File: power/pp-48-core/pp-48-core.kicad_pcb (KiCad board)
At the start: 4 copper layers, 56 x 72 mm, 74 parts, among them J1 XT30PW-M, J2 CTRL IN, J3 CTRL OUT, J301 CHAIN OUT, J4 12V AUX OUT, J5 SWD, Q1 2N7002, Q6 2N7002, U1 LM5164DDA, U2 URB4812YMD-6WR3, U3 STM32G070CBT6, U4 ISO1640BD, U5 ISO7721D, U6 TCA9548APWR, Y1 8MHz

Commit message: pp-48 plane boards: press deadline line (docs/press-deadline-line.md decided: option B + A) on a 14-pin chain (S14B-PH-K-S C157938; 13 PRESS_EN, 14 EXP_RSTN, cable n -> 15 - n, pins v 35..61); unit Q10 / R31 switch the photoMOS LED returns (PRESS_RTN), core U301 74LVC1G123 deadline (pp:74LVC1G123 single-unit copy) on PC6 PRESS_TRIG, PC7 EXP_RSTN to the units' /RESET; ERC 0 both; boards rebuilt and placed, unit 78.5 x 72 with the strip power path re-placed top-down; unit routing tools (route_unit.py hand copper + In2 band / +3V3 trunk, unitsplit.py, route_unit.sh flow): DRC 0 errors, ~10 unconnected at expander U5; core placed, not routed; pmmount.py restored from granite_controller; ADR 0005 decision 4; handoff
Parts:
- added C301: 10u, Capacitor_SMD:C_0805_2012Metric, F.Cu at (95.0, 163.6)
- added C302: 100n, Capacitor_SMD:C_0402_1005Metric, F.Cu at (95.0, 157.2)
- added R301: 100k, Resistor_SMD:R_0402_1005Metric, F.Cu at (98.6, 160.0)
- added R302: 100k, Resistor_SMD:R_0402_1005Metric, F.Cu at (91.6, 159.4)
- added R303: 10k, Resistor_SMD:R_0402_1005Metric, F.Cu at (91.6, 162.6)
- added U301: 74LVC1G123, Package_SO:SSOP-8_2.95x2.8mm_P0.65mm, F.Cu at (95.0, 160.0)
- J301: footprint Connector_JST:JST_PH_S12B-PH-K_1x12_P2.00mm_Horizontal -> Connector_JST:JST_PH_S14B-PH-K_1x14_P2.00mm_Horizontal
- moved J301 4.00 mm to (101.4, 135.0)
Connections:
- J301 pad 1: /UNIT4_SCL -> /EXP_RSTN
- J301 pad 10: /UNIT1_SCL -> /UNIT2_SDA
- J301 pad 11: /UNIT1_SDA -> GND
- J301 pad 12: +3V3 -> /UNIT1_SCL
- J301 pad 2: /UNIT4_SDA -> /Chain/PRESS_EN
- J301 pad 3: GND -> /UNIT4_SCL
- J301 pad 4: /UNIT3_SCL -> /UNIT4_SDA
- J301 pad 5: /UNIT3_SDA -> GND
- J301 pad 6: GND -> /UNIT3_SCL
- J301 pad 7: /UNIT2_SCL -> /UNIT3_SDA
- J301 pad 8: /UNIT2_SDA -> GND
- J301 pad 9: GND -> /UNIT2_SCL
- U3 pad 30: unconnected-(U3-PC6-Pad30) -> /PRESS_TRIG
- U3 pad 31: unconnected-(U3-PC7-Pad31) -> /EXP_RSTN

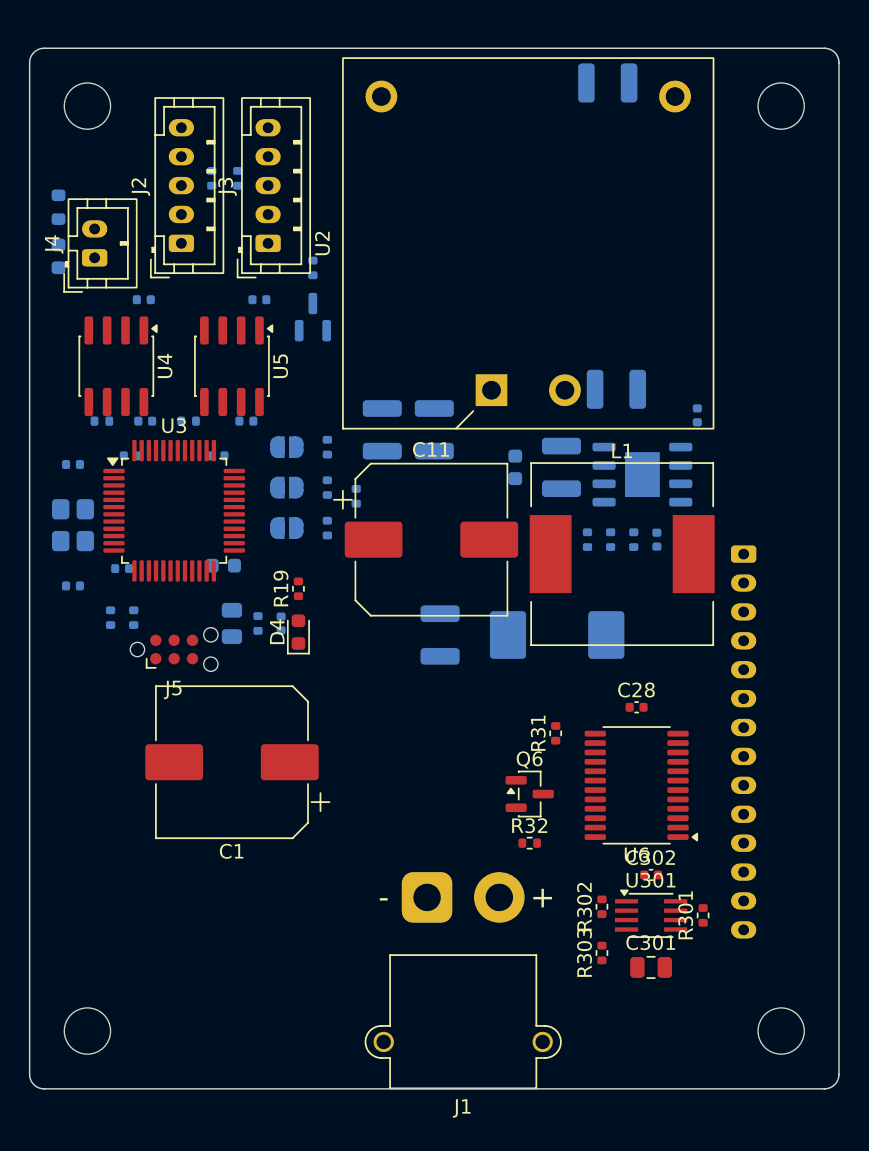
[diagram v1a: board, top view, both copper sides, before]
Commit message: pp-48-core: Fly-Buck placed where the 12 V module was (top right): L2 SRF0703 rot 270 on the corner of a new CTRL_GND island strip along the top edge (diagonal windings: SEC2 in the strip, SW / VOUT1 bus side, CTRL_GND pad an F pocket with vias to In1 / B), secondary D6 / C30 / C31 / D7 in the strip, U2 rot 180 with SW next to L2, its caps and networks on F / B around it; placement DRC 0 errors besides unconnected, parity clean; handoff
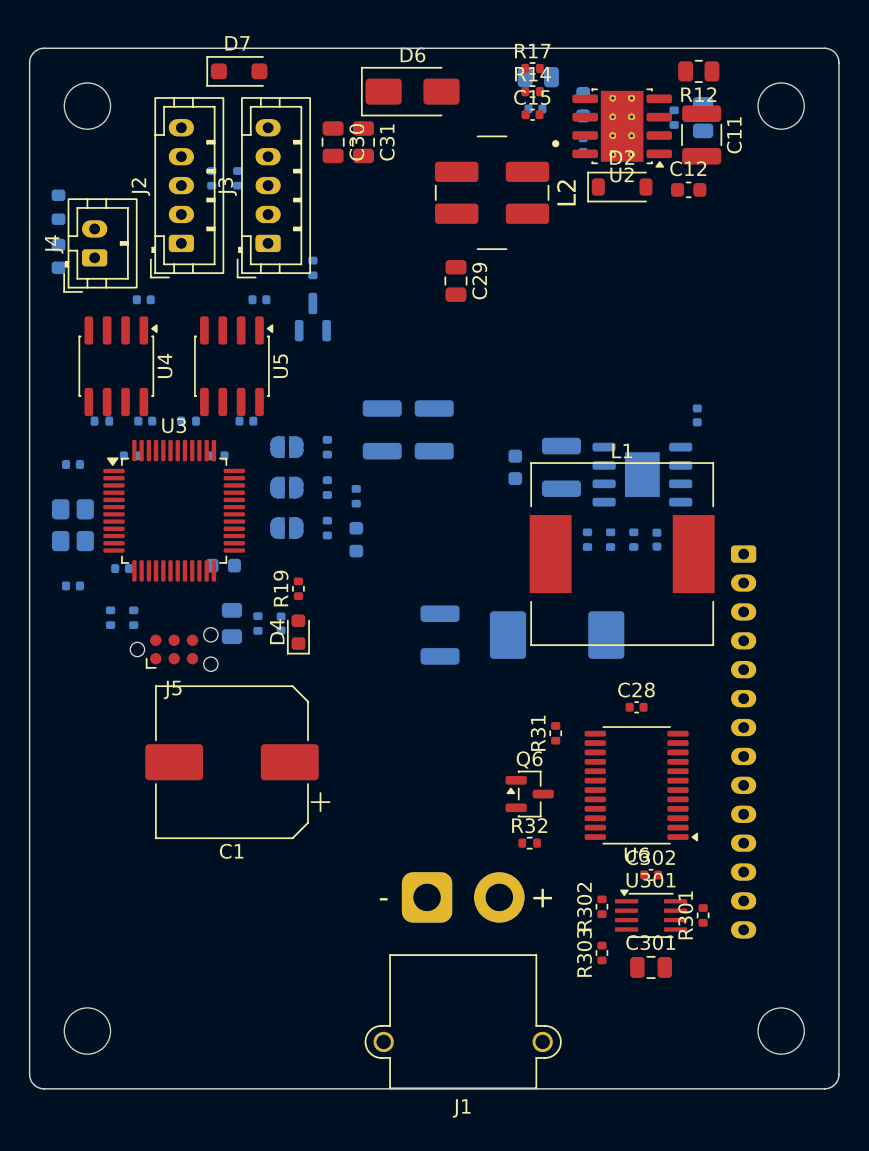
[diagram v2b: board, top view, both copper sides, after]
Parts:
- added C14: 1n, Capacitor_SMD:C_0402_1005Metric, B.Cu at (87.0, 104.2)
- added C15: 100n, Capacitor_SMD:C_0402_1005Metric, F.Cu at (86.8, 104.6)
- added C16: 1u 25V, Capacitor_SMD:C_0603_1608Metric, B.Cu at (90.3, 103.9)
- added C29: 4.7u 25V, Capacitor_SMD:C_0805_2012Metric, F.Cu at (81.5, 116.1)
- added C30: 10u 25V, Capacitor_SMD:C_0805_2012Metric, F.Cu at (73.0, 106.5)
- added C31: 10u 25V, Capacitor_SMD:C_0805_2012Metric, F.Cu at (75.1, 106.5)
- added D2: 1N4148W, Diode_SMD:D_SOD-123, F.Cu at (93.0, 109.6)
- added D6: SS110, Diode_SMD:D_SMA, F.Cu at (78.5, 103.0)
- added D7: SMF13A, Diode_SMD:D_SOD-123F, F.Cu at (66.5, 101.6)
- added L2: 47u, pp48:L_Bourns_SRF0703, F.Cu at (84.0, 110.0)
- added R10: 100k, Resistor_SMD:R_0805_2012Metric, B.Cu at (98.6, 104.8)
- added R11: 4.22k, Resistor_SMD:R_0402_1005Metric, B.Cu at (96.6, 104.8)
- added R12: 280k, Resistor_SMD:R_0805_2012Metric, F.Cu at (98.3, 101.6)
- added R13: 200k, Resistor_SMD:R_0805_2012Metric, B.Cu at (87.2, 102.0)
- added R14: 18.7k, Resistor_SMD:R_0402_1005Metric, F.Cu at (86.8, 103.0)
- added R17: 2k, Resistor_SMD:R_0402_1005Metric, F.Cu at (86.8, 101.4)
- C11: value 22u 100V -> 2.2u 100V; footprint Capacitor_SMD:CP_Elec_10x10 -> Capacitor_SMD:C_1210_3225Metric
- C12: value 2.2u 100V -> 100n 100V; footprint Capacitor_SMD:C_1210_3225Metric -> Capacitor_SMD:C_0603_1608Metric; moved to F.Cu
- C13: value 10u 50V -> 10n 50V; footprint Capacitor_SMD:C_1210_3225Metric -> Capacitor_SMD:C_0402_1005Metric
- U2: value URB4812YMD-6WR3 -> LM5017MRX/NOPB; footprint pp48:Converter_DCDC_1x1in_THT -> Package_SO:SOIC-8-1EP_3.9x4.9mm_P1.27mm_EP2.95x4.9mm_Mask2.71x3.4mm_ThermalVias
- moved C11 33.7 mm to (98.5, 106.0), turned to -90 degrees
- moved C12 14.7 mm to (97.6, 109.8)
- moved U2 10.4 mm to (93.0, 105.4), turned to 180 degrees
- moved C13 4.62 mm to (90.3, 106.7), turned to 90 degrees
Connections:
- C13 pad 1: CTRL_12V -> /Supplies/BST2
- C13 pad 2: CTRL_GND -> /Supplies/SW2
- U2 pad 3: CTRL_12V -> /Supplies/UVLO2
- U2 pad 5: CTRL_GND -> /Supplies/FB2

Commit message: pp-48-core: routed (DRC 0 unconnected, parity clean; isocheck: no island copper within 1 mm of the bus world): tools/route_core.py draws the CTRL_GND island pours, L2's CTRL_GND pocket with its vias to In1 / B, the island under L2, the per-layer isolation bands and the Fly-Buck SW track (0.6 mm, U2 -> L2); route_core.sh runs it with krt-route (VIN plane on In2), reroute passes, mazefix, prune, mergetracks and the fill; tools/isocheck.py checks the island clearance; crystal Y1 turned (no OSC crossing), two starved GND pads solid; handoff
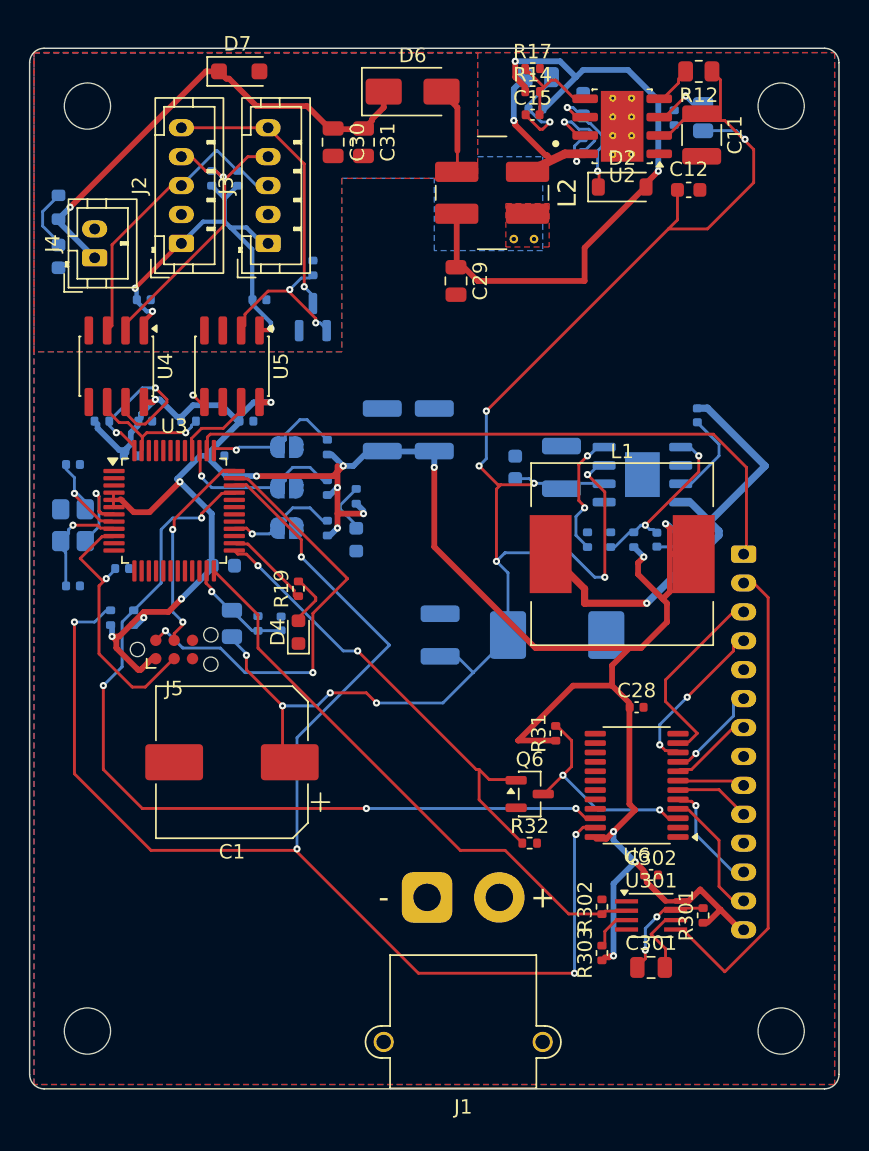
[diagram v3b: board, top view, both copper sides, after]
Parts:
- added CV1: , , F.Cu at (85.5, 113.2)
- added CV2: , , F.Cu at (86.9, 113.2)
- turned Y1 to -90 degrees
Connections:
- U3 pad 1: /MCU/ADR0 -> unconnected-(U3-PC13-Pad1)
- U3 pad 19: /VIN_SNS -> unconnected-(U3-PB0-Pad19)
- U3 pad 2: /MCU/ADR1 -> unconnected-(U3-PC14-Pad2)
- U3 pad 22: /SCL2 -> unconnected-(U3-PB10-Pad22)
- U3 pad 23: /SDA2 -> /VIN_SNS
- U3 pad 24: /MUX_RST -> /PRESS_TRIG
- U3 pad 25: unconnected-(U3-PB13-Pad25) -> /MUX_RST
- U3 pad 26: unconnected-(U3-PB14-Pad26) -> /MCU/LED_RUN
- U3 pad 28: /INT_OUT -> /MCU/ADR2
- U3 pad 3: /MCU/ADR2 -> unconnected-(U3-PC15-Pad3)
- U3 pad 30: /PRESS_TRIG -> unconnected-(U3-PC6-Pad30)
- U3 pad 31: /EXP_RSTN -> unconnected-(U3-PC7-Pad31)
- U3 pad 33: unconnected-(U3-PA9/PA11-Pad33) -> /SCL2
- U3 pad 34: unconnected-(U3-PA10/PA12-Pad34) -> /SDA2
- U3 pad 37: unconnected-(U3-PA15-Pad37) -> /MCU/ADR0
- U3 pad 38: unconnected-(U3-PD0-Pad38) -> /EXP_RSTN
- U3 pad 39: unconnected-(U3-PD1-Pad39) -> /MCU/ADR1
- U3 pad 40: unconnected-(U3-PD2-Pad40) -> /INT_OUT
- U3 pad 45: /SCL1 -> unconnected-(U3-PB6-Pad45)
- U3 pad 46: /SDA1 -> unconnected-(U3-PB7-Pad46)
- U3 pad 47: /MCU/LED_RUN -> /SCL1
- U3 pad 48: unconnected-(U3-PB9-Pad48) -> /SDA1
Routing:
- net +3V3: track 0.00 -> 165.4 mm, vias 0 -> 17
- net VIN: track 0.00 -> 106.2 mm, vias 0 -> 9
- net /SDA2: track 0.00 -> 97.1 mm, vias 0 -> 5
- net /SCL2: track 0.00 -> 59.4 mm, vias 0 -> 4
- net /EXP_RSTN: track 0.00 -> 45.1 mm
- net /Supplies/VOUT1: track 0.00 -> 43.4 mm, vias 0 -> 2
- net /PRESS_TRIG: track 0.00 -> 39.2 mm
- net CTRL_12V: track 0.00 -> 33.2 mm, vias 0 -> 1
- net /Chain/PRESS_EN: track 0.00 -> 32.7 mm
- net /MUX_RST: track 0.00 -> 32.4 mm, vias 0 -> 2
- net /MCU/SWDIO: track 0.00 -> 30.5 mm, vias 0 -> 2
- net /Supplies/SW1: track 0.00 -> 30.5 mm, vias 0 -> 1
- net CTRL_3V3: track 0.00 -> 27.1 mm, vias 0 -> 3
- net /Link/CTRL_SDA: track 0.00 -> 20.0 mm, vias 0 -> 1
- net /Link/CTRL_SCL: track 0.00 -> 18.7 mm
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- added copper zone on B.Cu, net CTRL_GND
- added copper zone on F.Cu, net CTRL_GND
- added copper zone on In1.Cu, net CTRL_GND
- added copper zone on B.Cu, net GND
- added copper zone on F.Cu, net GND
- added copper zone on In1.Cu, net GND
- added copper zone on In2.Cu, net VIN

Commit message: pp-48-core: GND stitch (1 via), silk (23 refs placed, 71 small ones hidden), JLC outputs; LCSC codes for the 25 passive values that had none (sch/draw.py BASIC table, JLC parts API: basic where JLC has one), copied onto the routed board; BOM 86 parts, left out only CV1/CV2, holes, J5 / JP1-3 (copper only) and DNP R28 / R29; DRC 0 unconnected, parity clean, isocheck clean
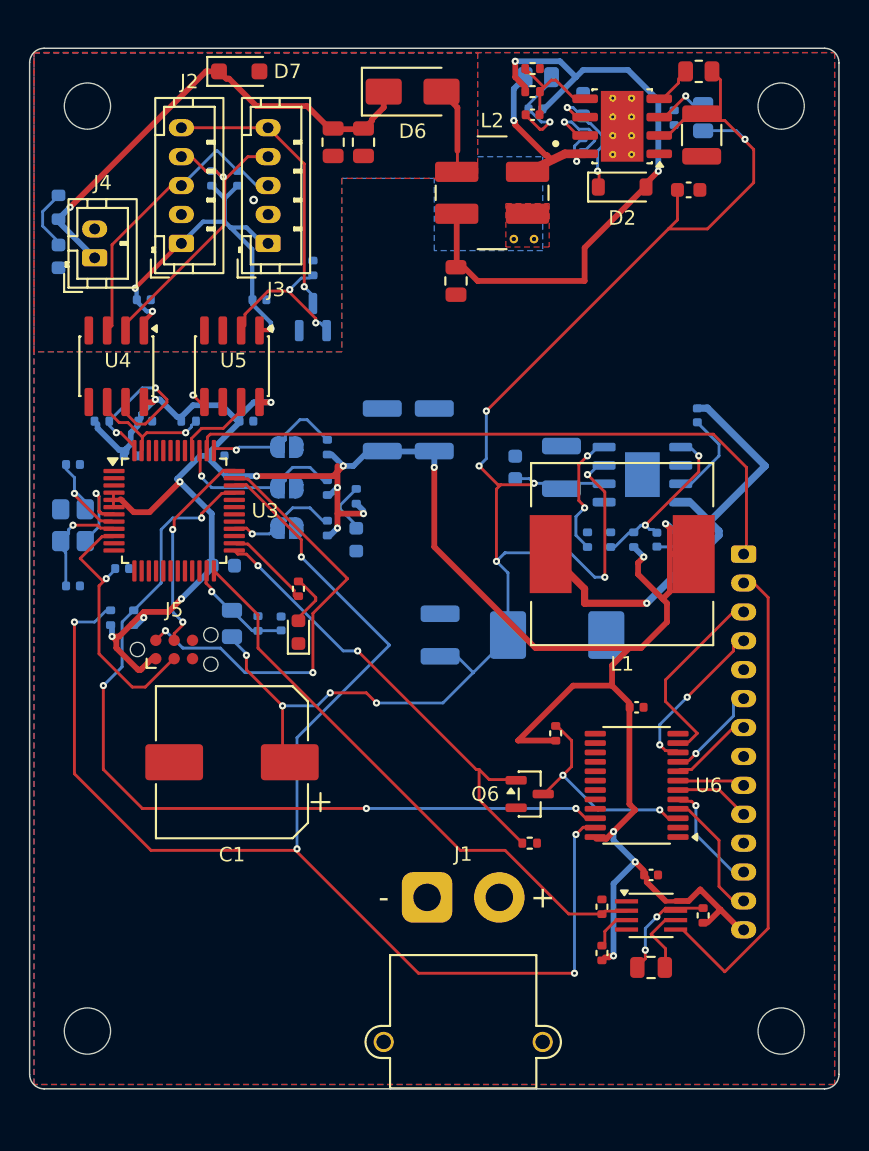
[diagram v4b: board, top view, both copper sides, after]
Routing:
- net CTRL_GND: vias 0 -> 1

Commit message: pp-48-core J1: project footprint pp48:AMASS_XT30PW-M (the stock one points to a STEP KiCad does not ship) with the LCSC / EasyEDA model C431092 (pp48.3dshapes), turned 180 and offset (-2.5, 8.48) to sit on the pins and pegs (checked in a top / bottom render); J1 on the routed board updated in place; ERC 0, DRC unchanged
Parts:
- J1: footprint Connector_AMASS:AMASS_XT30PW-M_1x02_P2.50mm_Horizontal -> pp48:AMASS_XT30PW-M_1x02_P2.50mm_Horizontal
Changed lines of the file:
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@@
 		(embedded_fonts no)
 	)
-	(footprint "Connector_AMASS:AMASS_XT30PW-M_1x02_P2.50mm_Horizontal"
+	(footprint "pp48:AMASS_XT30PW-M_1x02_P2.50mm_Horizontal"
 		(layer "F.Cu")
 		(at 79.5 158.755 180)
@@
 		)
 		(embedded_fonts no)
-		(model "${KICAD10_3DMODEL_DIR}/Connector_AMASS.3dshapes/AMASS_XT30PW-M_1x02_P2.50mm_Horizontal.step"
+		(model "${KIPRJMOD}/../pp-48/pp48.3dshapes/AMASS_XT30PW-M.step"
 			(offset
-				(xyz 0 0 0)
+				(xyz -2.5 8.48 0)
 			)
 			(scale
@@
 			)
 			(rotate
-				(xyz 0 0 0)
-			)
-		)
+				(xyz 0 0 180)
+			)
+		)

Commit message: pp-48-core 12 V aux: LM5018 + Coilcraft LPD5030V-333 replace the LM5017 + SRF0703 (ADR 0003 decision 14 revised): the SRF0703's real land pattern puts its windings' pads 0.46 mm apart with no isolation rating; the LPD5030V (4.8 x 4.8 mm, 1000 V winding to winding) has one winding per side, so the island barrier is straight (1.48 mm under the part), no pocket or vias; ~1.2 W, RON 169k (~800 kHz); footprint pp48:L_Coilcraft_LPD5030V from Coilcraft's land pattern with the LCSC 3D model; re-placed, routed, U2 exposed pad solid, gnd stitch, silk, JLC outputs. 3D models: L1 on Inductor_SMD:L_Bourns_SRR1260 (the part, SRR1260-330M; pads 0.1 mm further in than the generic 12x12, stock model), U2 on a project copy of its SOIC-8-1EP footprint pointing at the stock EP2.41x3.81 STEP (the referenced one is not shipped); both swapped on the routed board in place. ERC 0, DRC 0 unconnected, parity clean, isocheck clean, BOM 86 parts; handoff
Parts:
- removed CV1, CV2: , 
- L1: footprint Inductor_SMD:L_12x12mm_H6mm -> Inductor_SMD:L_Bourns_SRR1260
- L2: value 47u -> 33u; footprint pp48:L_Bourns_SRF0703 -> pp48:L_Coilcraft_LPD5030V
- R12: value 280k -> 169k
- R17: moved to B.Cu
- U2: value LM5017MRX/NOPB -> LM5018MRX/NOPB; footprint Package_SO:SOIC-8-1EP_3.9x4.9mm_P1.27mm_EP2.95x4.9mm_Mask2.71x3.4mm_ThermalVias -> pp48:SOIC-8-1EP_3.9x4.9mm_P1.27mm_EP2.95x4.9mm_Mask2.71x3.4mm_ThermalVias
- moved C29 16.0 mm to (87.4, 101.2), turned to 0 degrees
- moved R17 5.46 mm to (87.6, 106.8)
- moved L2 5.00 mm to (84.0, 105.0), turned to 180 degrees
- moved C15 2.01 mm to (88.6, 103.7), turned to 90 degrees
- moved R14 0.92 mm to (87.4, 103.7), turned to 90 degrees
- moved D6 0.90 mm to (77.6, 103.0)
- moved C30 0.20 mm to (73.0, 106.7)
- moved C31 0.20 mm to (75.1, 106.7)
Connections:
- L2 pad 2: CTRL_GND -> /Supplies/VOUT1
- L2 pad 3: /Supplies/VOUT1 -> /Supplies/SEC2
- L2 pad 4: /Supplies/SEC2 -> CTRL_GND
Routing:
- net /Supplies/VOUT1: track 43.4 -> 17.4 mm
- net /Supplies/FB2: track 6.58 -> 22.1 mm, vias 0 -> 1
- net VIN: track 106.2 -> 94.2 mm, vias 9 -> 8
- net /PRESS_TRIG: track 39.2 -> 46.4 mm
- net /SDA1: track 11.6 -> 4.50 mm, vias 2 -> 1
- net /Supplies/VCC2: track 7.80 -> 14.1 mm, vias 2 -> 3
- net GND: track 7.65 -> 2.81 mm
- net /SCL1: track 8.26 -> 12.6 mm
- net /Supplies/SEC2: track 6.06 -> 2.05 mm
- net /SCL2: track 59.4 -> 55.6 mm
- net /SDA2: track 97.1 -> 94.1 mm
- net /MUX_RST: track 32.4 -> 35.0 mm, vias 2 -> 0
- net /Supplies/SW2: track 13.3 -> 11.0 mm
- net /MCU/SWDIO: track 30.5 -> 32.3 mm
- net +3V3: track 165.4 -> 167.1 mm
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
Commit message: pp-48-core address straps: solder jumpers JP1-3 -> 3-way SMD DIP switch SW1 (KingTek DSHP03TSGET, C50844, 1.27 mm pitch, KiCad footprint and model) on F right of U3, ON = 0, plane address 0x30 + ADR[2:0]; swapped on the routed board (ADR0-2, +3V3 and SWDIO rerouted with krt-reroute --keep, one mazefix GND hop, mergetracks, silk, fill), core.py table updated for a rebuild; ERC 0, DRC 0 unconnected, parity clean, isocheck clean, BOM 87 parts; handoff
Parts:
- removed JP1: ADR0, Jumper:SolderJumper-2_P1.3mm_Open_RoundedPad1.0x1.5mm
- removed JP2: ADR1, Jumper:SolderJumper-2_P1.3mm_Open_RoundedPad1.0x1.5mm
- removed JP3: ADR2, Jumper:SolderJumper-2_P1.3mm_Open_RoundedPad1.0x1.5mm
- added SW1: ADR, Button_Switch_SMD:SW_DIP_SPSTx03_Slide_KingTek_DSHP03TS_W7.62mm_P1.27mm, F.Cu at (73.6, 130.4)
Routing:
- net /MCU/SWDIO: track 32.3 -> 19.7 mm, vias 2 -> 0
- net +3V3: track 167.1 -> 170.8 mm, vias 17 -> 15
- net GND: track 2.81 -> 6.00 mm, vias 2 -> 3
- net /MCU/ADR0: track 9.28 -> 8.04 mm
- net /MCU/ADR1: track 12.1 -> 12.7 mm, vias 1 -> 3
- net /MCU/NRST: track 18.4 -> 17.9 mm
- net /MCU/ADR2: track 7.42 -> 6.95 mm, vias 1 -> 3

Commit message: pp-48-core SWD: J6 ARM Cortex 10-pin header (Samtec FTSH-105-01-L-DV-K, C5155080, keyed shroud) on F right of U3 below SW1, for stock probe ribbons; the Tag-Connect pads J5 stay; J6 drawn as Conn_02x05 (two ARM SWD symbols on one net are output-to-output in ERC); SWDIO / SWCLK / NRST / +3V3 routed with krt-reroute --keep, silk, fill; ERC 0, DRC 0 unconnected, parity clean, isocheck clean, BOM 88 parts; handoff
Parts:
- added J6: SWD, Connector_PinHeader_1.27mm:PinHeader_2x05_P1.27mm_Vertical_SMD, F.Cu at (77.0, 139.5)
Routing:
- net /MCU/NRST: track 17.9 -> 47.8 mm, vias 1 -> 3
- net /MCU/SWCLK: track 14.0 -> 30.9 mm, vias 2 -> 6
- net /MCU/SWDIO: track 19.7 -> 34.6 mm, vias 0 -> 2
- net +3V3: track 170.8 -> 175.9 mm, vias 15 -> 17
